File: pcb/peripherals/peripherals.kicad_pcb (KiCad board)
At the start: 2 copper layers, 77 x 64.5 mm, 42 parts, among them J1 JST XH, J10 Conn_01x04, J2 JST XH, J3 JST XH, J4 Conn_01x08, J5 JST XH, J6 JST XH, J7 JST XH, J8 JST XH, J9 Conn_01x08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

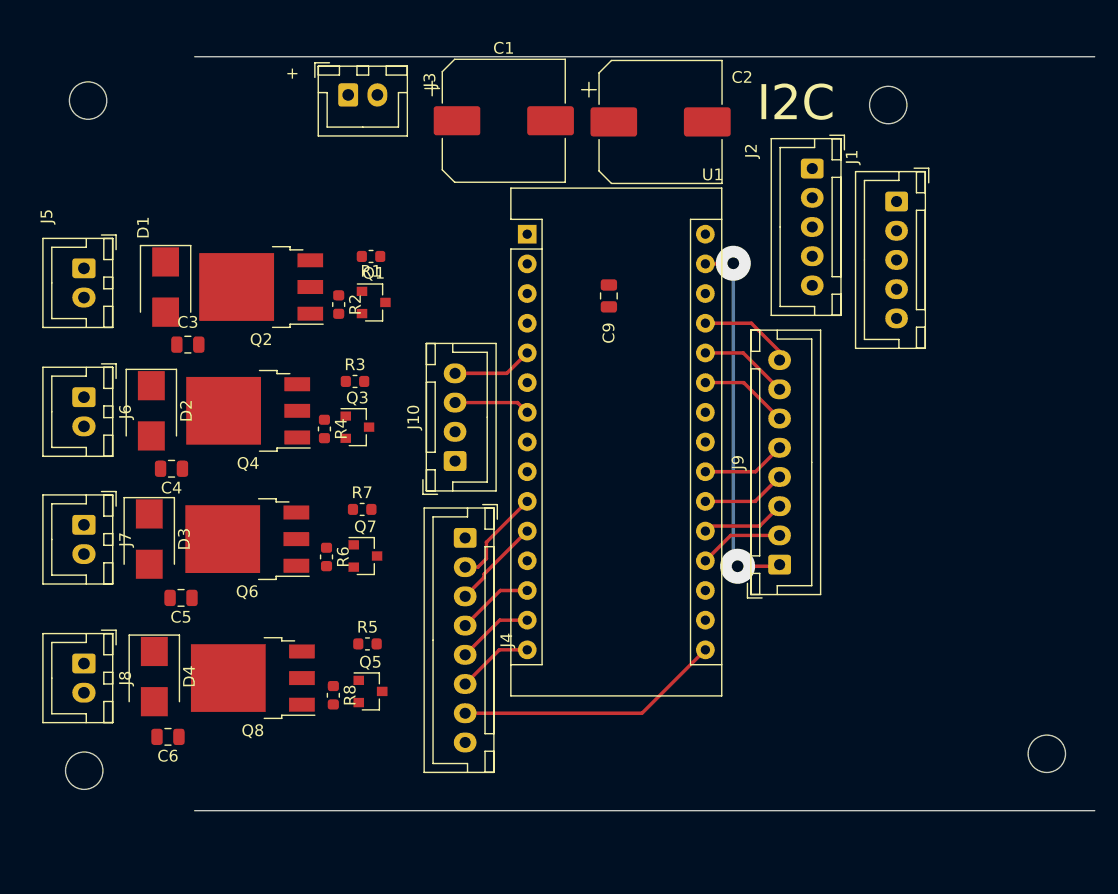
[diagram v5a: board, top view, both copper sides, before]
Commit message: Finish routing.
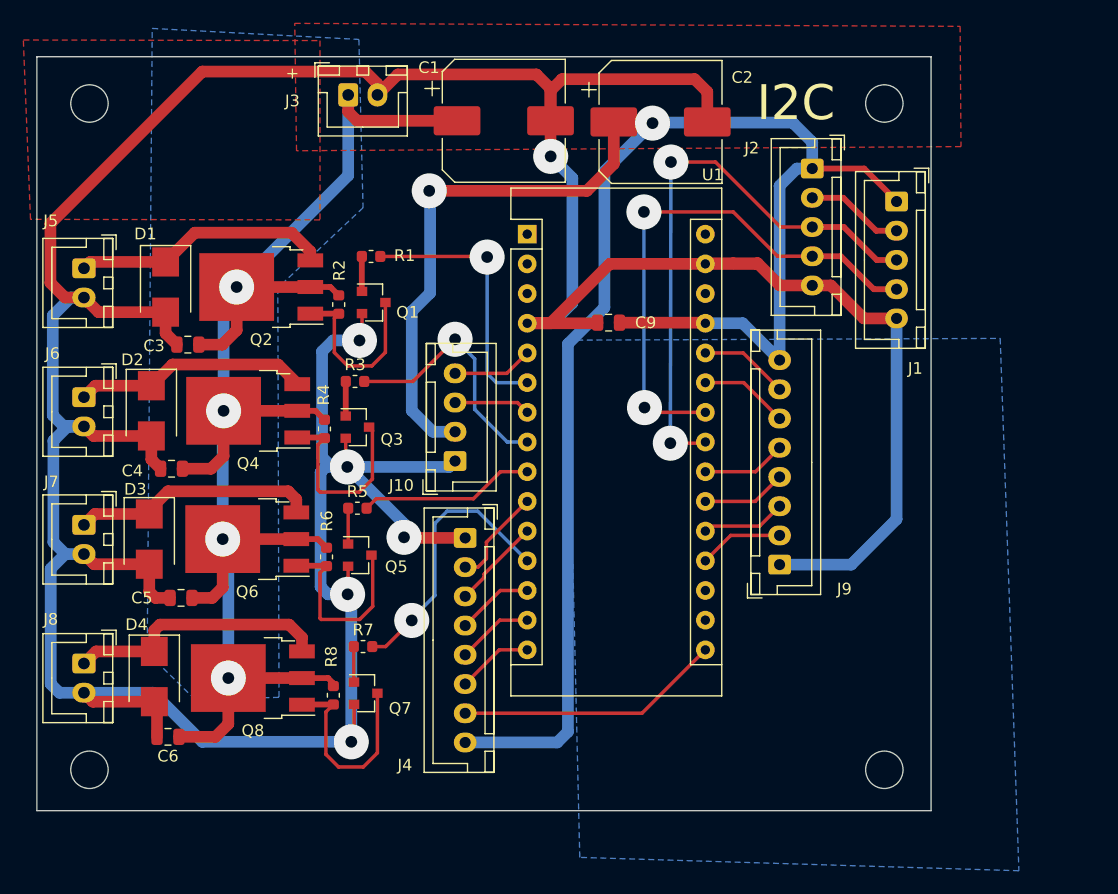
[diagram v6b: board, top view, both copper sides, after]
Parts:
- moved H1 14.0 mm to (75.0, 89.0)
- moved R7 11.7 mm to (30.4, 78.5)
- moved Q7 11.7 mm to (30.6, 82.4)
- moved Q5 11.7 mm to (30.1, 70.6)
- moved R5 11.6 mm to (29.9, 66.6)
- moved C9 2.29 mm to (51.4, 50.7), turned to 0 degrees
- moved H2 0.45 mm to (7.00, 89.0)
- moved H3 0.36 mm to (75.0, 32.0)
- moved H4 0.28 mm to (7.00, 32.0)
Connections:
- Q1 pad 2: Net-(Q1-Pad2) -> GND
- Q1 pad 3: GND -> Net-(Q1-Pad3)
- Q2 pad 1: Net-(Q1-Pad2) -> Net-(Q1-Pad3)
- Q3 pad 2: Net-(Q3-Pad2) -> GND
- Q3 pad 3: GND -> Net-(Q3-Pad3)
- Q4 pad 1: Net-(Q3-Pad2) -> Net-(Q3-Pad3)
- Q5 pad 2: Net-(Q5-Pad2) -> GND
- Q5 pad 3: GND -> Net-(Q5-Pad3)
- Q6 pad 1: Net-(Q5-Pad2) -> Net-(Q5-Pad3)
- Q7 pad 2: Net-(Q7-Pad2) -> GND
- Q7 pad 3: GND -> Net-(Q7-Pad3)
- Q8 pad 1: Net-(Q7-Pad2) -> Net-(Q7-Pad3)
- R2 pad 2: Net-(Q1-Pad2) -> Net-(Q1-Pad3)
- R4 pad 2: Net-(Q3-Pad2) -> Net-(Q3-Pad3)
- R6 pad 2: Net-(Q5-Pad2) -> Net-(Q5-Pad3)
- R8 pad 2: Net-(Q7-Pad2) -> Net-(Q7-Pad3)
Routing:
- net GND: track 32.1 -> 366.7 mm, vias 2 -> 6
- net +5V: track 8.09 -> 171.0 mm, vias 0 -> 2
- net +24V: track 0.00 -> 133.2 mm, vias 0 -> 4
- net SDA: track 0.00 -> 49.9 mm, vias 0 -> 2
- net SCL: track 0.00 -> 46.5 mm, vias 0 -> 2
- net PWM4: track 0.00 -> 23.5 mm, vias 0 -> 1
- net PWM1: track 0.00 -> 22.9 mm, vias 0 -> 1
- net Net-(D4-Pad1): track 0.00 -> 22.7 mm
- net Net-(D1-Pad1): track 0.00 -> 22.1 mm
- net PWM2: track 0.00 -> 21.6 mm, vias 0 -> 1
- net Net-(D3-Pad1): track 0.00 -> 21.0 mm
- net Net-(D2-Pad1): track 0.00 -> 20.1 mm
- net Net-(Q7-Pad3): track 0.00 -> 17.7 mm
- net Net-(Q3-Pad3): track 0.00 -> 16.8 mm
- net Net-(Q5-Pad3): track 0.00 -> 16.7 mm
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- added copper zone on B.Cu, net +24V
- added copper zone on B.Cu, net GND
- added copper zone on F.Cu, net GND
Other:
- board size 77 x 64.5 mm -> 76.5 x 64.5 mm
- rule pad_to_mask_clearance: 0.051 -> 0

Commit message: Update.
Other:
- net class Default removed

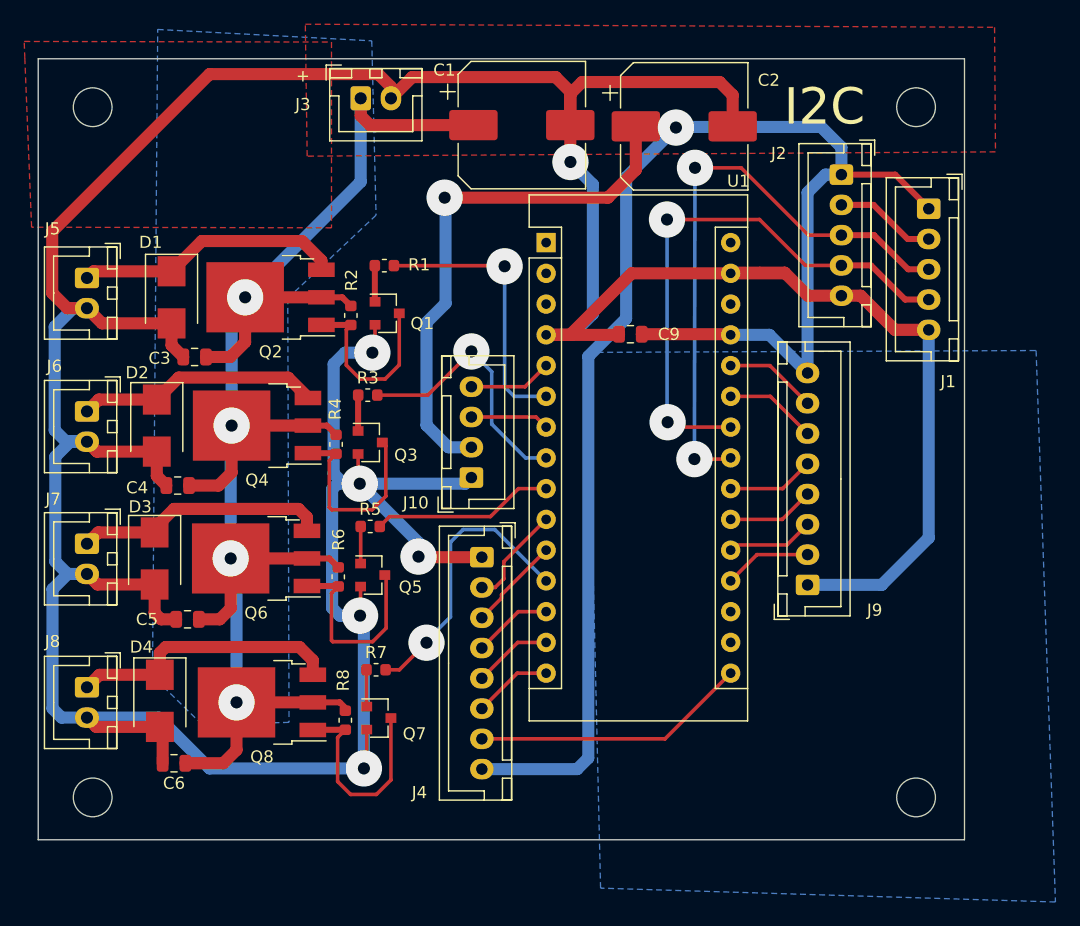
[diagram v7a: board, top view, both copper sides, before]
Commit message: Fix MOSFET polarity.
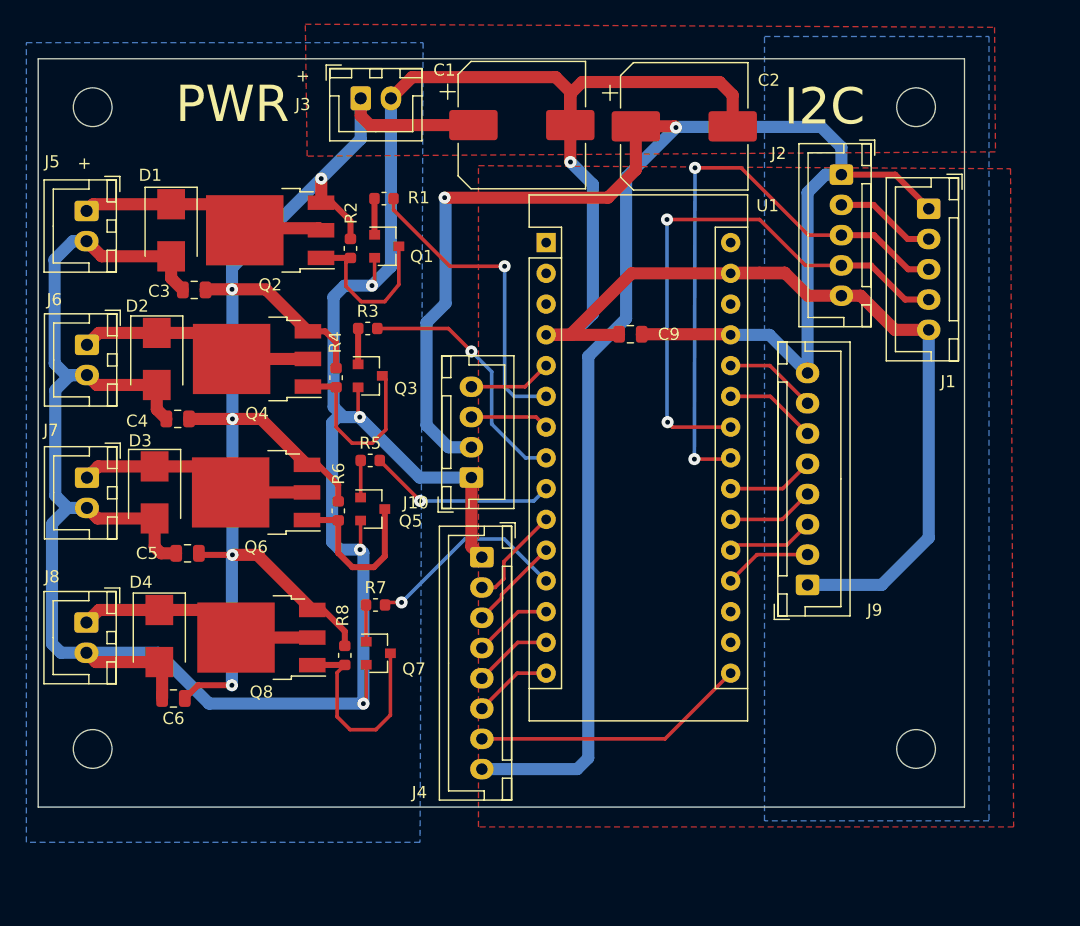
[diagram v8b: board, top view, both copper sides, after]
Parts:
- moved R2 5.54 mm to (28.3, 43.7)
- moved C3 5.54 mm to (15.4, 47.1)
- moved D1 5.54 mm to (13.5, 42.2)
- moved J5 5.54 mm to (6.49, 40.6)
- moved Q1 5.54 mm to (31.3, 43.5)
- moved Q2 5.54 mm to (21.7, 42.2)
- moved R1 5.54 mm to (31.1, 39.5)
- moved C4 5.50 mm to (14.0, 57.7)
- moved J6 5.50 mm to (6.53, 51.6)
- moved D2 5.50 mm to (12.3, 52.8)
- moved Q3 5.50 mm to (29.9, 54.2)
- moved Q4 5.50 mm to (20.6, 52.8)
- moved R3 5.50 mm to (29.7, 50.3)
- moved R4 5.50 mm to (27.1, 54.3)
- moved C5 5.45 mm to (14.8, 68.8)
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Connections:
- Q2 pad 2: +24V -> Net-(D1-Pad1)
- Q2 pad 3: Net-(D1-Pad1) -> +24V
- Q4 pad 2: +24V -> Net-(D2-Pad1)
- Q4 pad 3: Net-(D2-Pad1) -> +24V
- Q6 pad 2: +24V -> Net-(D3-Pad1)
- Q6 pad 3: Net-(D3-Pad1) -> +24V
- Q8 pad 2: +24V -> Net-(D4-Pad1)
- Q8 pad 3: Net-(D4-Pad1) -> +24V
- U1 pad 1: Net-(U1-Pad1) -> unconnected-(U1-Pad1)
- U1 pad 17: Net-(U1-Pad17) -> unconnected-(U1-Pad17)
- U1 pad 18: Net-(U1-Pad18) -> unconnected-(U1-Pad18)
- U1 pad 2: Net-(U1-Pad2) -> unconnected-(U1-Pad2)
- U1 pad 28: Net-(U1-Pad28) -> unconnected-(U1-Pad28)
- U1 pad 3: Net-(U1-Pad3) -> unconnected-(U1-Pad3)
- U1 pad 30: Net-(U1-Pad30) -> unconnected-(U1-Pad30)
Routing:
- net GND: track 366.7 -> 335.6 mm, vias 6 -> 5
- net +24V: track 133.2 -> 121.2 mm, vias 4 -> 5
- net PWM4: track 23.5 -> 17.0 mm
- net PWM1: track 22.9 -> 25.8 mm
- net Net-(D4-Pad1): track 22.7 -> 20.0 mm
- net Net-(Q5-Pad3): track 16.7 -> 14.0 mm
- net Net-(Q1-Pad3): track 15.5 -> 13.6 mm
- net Net-(Q3-Pad3): track 16.8 -> 15.3 mm
- net Net-(D1-Pad1): track 22.1 -> 20.8 mm
- net Net-(D3-Pad1): track 21.0 -> 19.8 mm
- net PWM2: track 21.6 -> 20.9 mm
- net Net-(D2-Pad1): track 20.1 -> 19.5 mm
- net PWM3: track 15.0 -> 15.6 mm, vias 0 -> 1
- added copper zone on F.Cu, net +5V
- removed copper zone on B.Cu, net +24V
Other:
- board size 76.5 x 64.5 mm -> 76.5 x 61.8 mm
- board text added: "PWR"
